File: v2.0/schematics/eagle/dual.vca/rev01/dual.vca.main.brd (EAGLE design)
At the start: 86 x 99 mm, 92 parts, among them IC1 TL082P, IC2 TL084P, IC3 LM324N, T1 BC547, T2 BC547, T3 BC547, T4 BC547, T5 BC547, T6 BC547

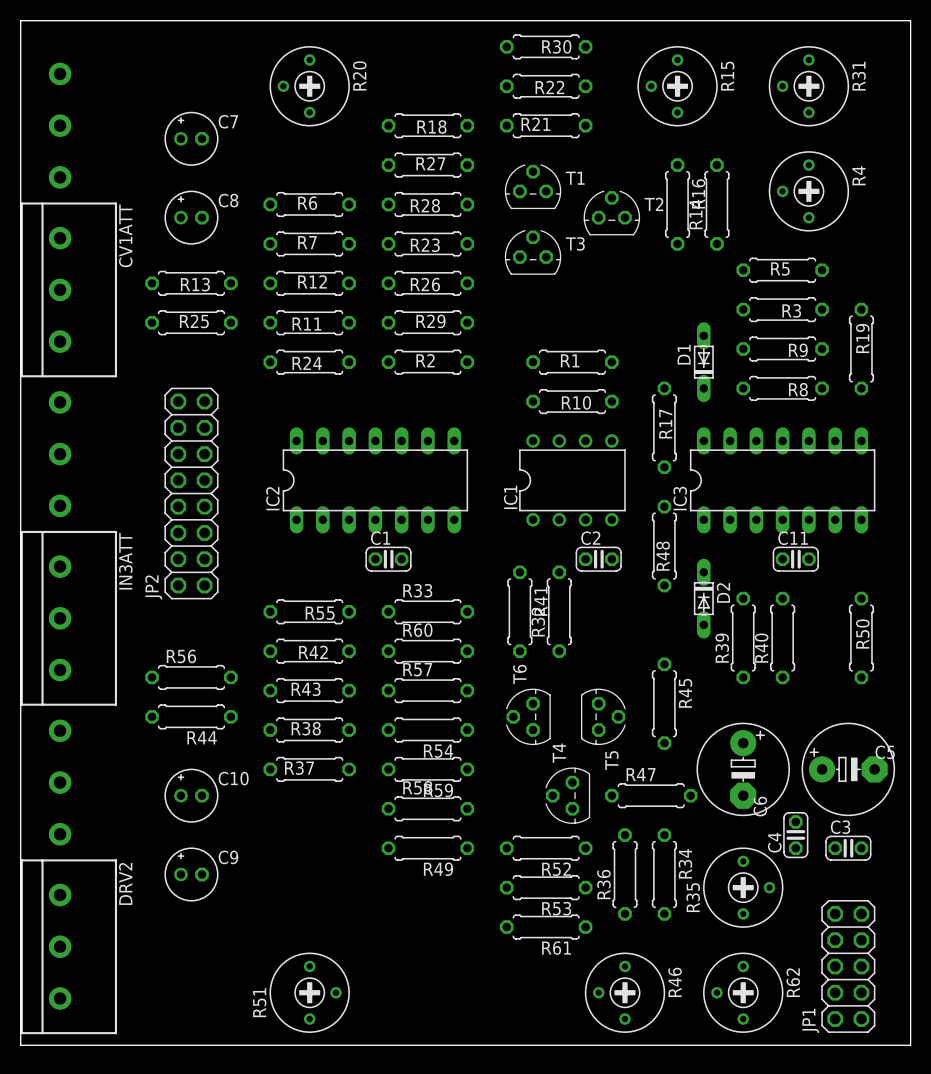
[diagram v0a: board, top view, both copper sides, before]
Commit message: Dual VCA autoroute and ground planes
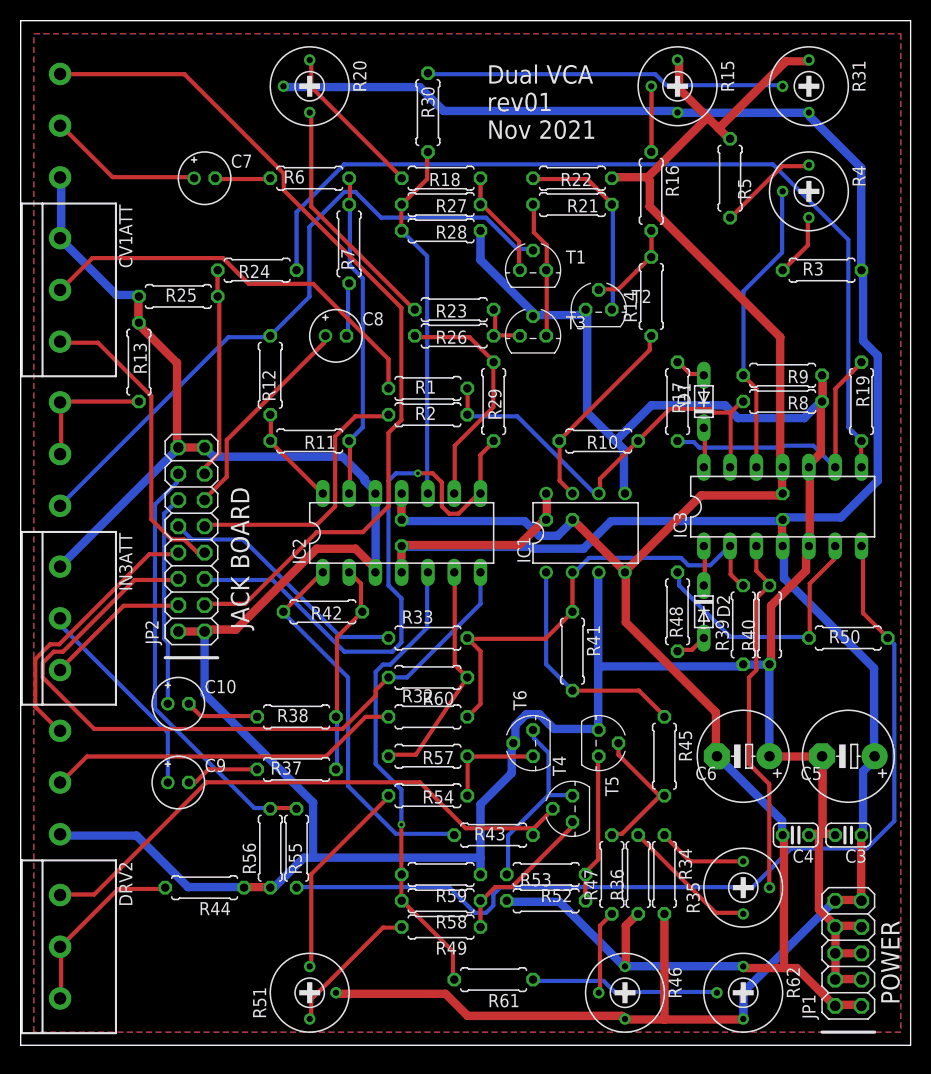
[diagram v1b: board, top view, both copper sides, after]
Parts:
- moved R55 22.9 mm to (26.7, 19.1), turned to 90 degrees
- moved R43 22.6 mm to (45.7, 20.3)
- moved R56 18.2 mm to (24.1, 19.1), turned to 90 degrees
- moved C8 18.1 mm to (30.5, 68.6)
- moved R44 16.6 mm to (17.8, 15.2)
- moved R32 16.3 mm to (39.4, 31.8), turned to 0 degrees
- moved R1 14.2 mm to (39.4, 63.5)
- moved R30 13.1 mm to (39.4, 90.2), turned to 270 degrees
- moved R11 11.4 mm to (27.9, 58.4)
- moved R14 10.9 mm to (61.0, 72.4)
- moved R24 10.2 mm to (22.9, 74.9)
- moved R59 10.2 mm to (40.6, 16.5)
- moved R5 10.2 mm to (68.6, 83.8), turned to 270 degrees
- moved R29 9.92 mm to (45.7, 62.2), turned to 270 degrees
- moved R12 9.67 mm to (24.1, 64.8), turned to 90 degrees
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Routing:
- net 0V: track 0.00 -> 362.5 mm
- net +12V: track 0.00 -> 268.6 mm
- net -12V: track 0.00 -> 204.0 mm
- net N$52: track 0.00 -> 91.1 mm
- net N$25: track 0.00 -> 86.4 mm
- net IN1: track 0.00 -> 84.8 mm
- net OUT3: track 0.00 -> 70.6 mm
- net N$4: track 0.00 -> 64.6 mm
- net OUT1: track 0.00 -> 57.1 mm, vias 0 -> 1
- net N$53: track 0.00 -> 55.5 mm
- net N$43: track 0.00 -> 45.1 mm
- net N$37: track 0.00 -> 45.1 mm, vias 0 -> 1
- net N$19: track 0.00 -> 42.6 mm
- net OUT4: track 0.00 -> 41.4 mm
- net N$29: track 0.00 -> 39.9 mm
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- added copper zone on layer 1, net 0V
- added copper zone on layer 16, net 0V
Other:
- board text added: "Dual VCA rev01 Nov 2021"
- board text added: "JACK BOARD"
- board text added: "POWER"

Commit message: Adjusted Dual.Seq comparrator
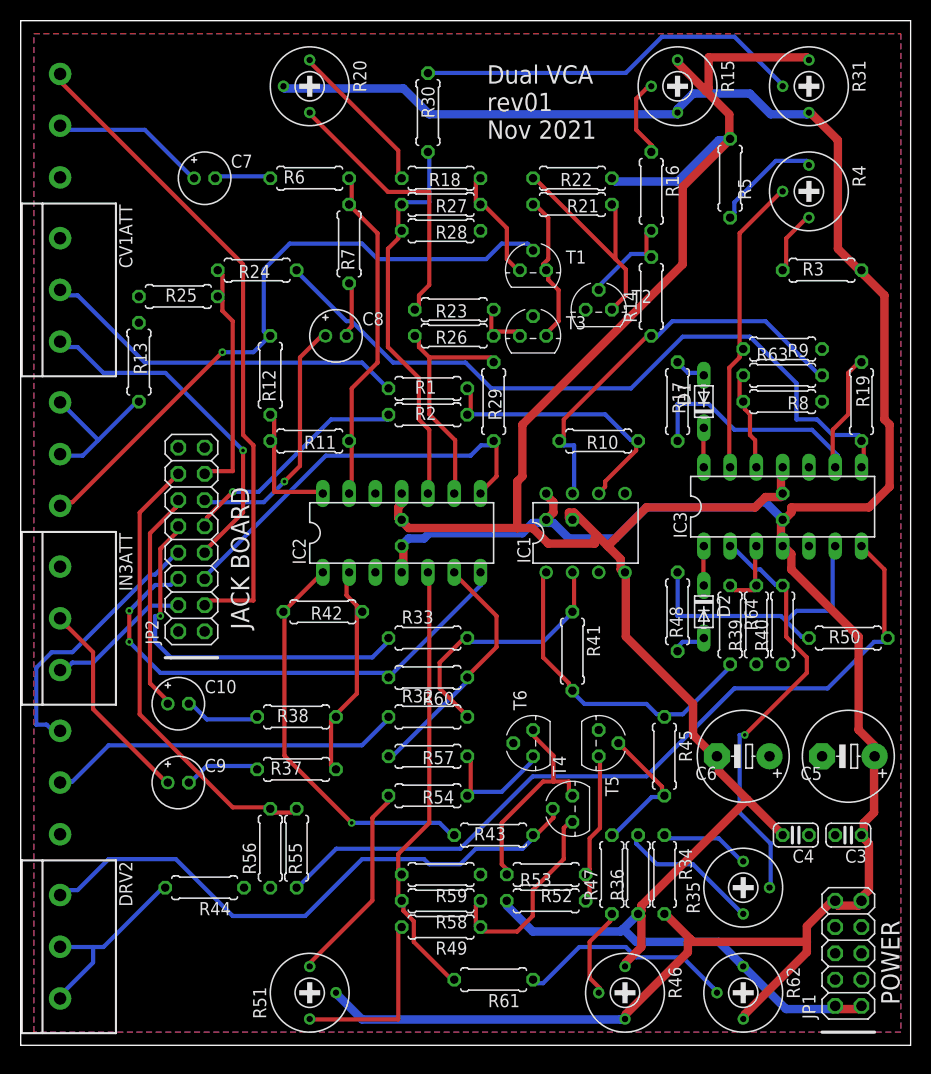
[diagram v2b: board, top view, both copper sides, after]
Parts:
- added R63, R64: 100K, _common:0207/7
- R1, R32: value 100K -> 65K
- moved R9 2.54 mm to (73.7, 67.3)
- moved R39 1.27 mm to (71.1, 40.6)
- moved R40 1.27 mm to (73.7, 40.6)
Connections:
- new net N$57: IC3.12, R63.1, R8.2
- new net N$58: IC3.2, R35.2, R40.2
- net N$17: now also R63.2
- net N$18: now also IC3.13; no longer IC3.12
- net N$19: no longer IC3.13, R8.2
- net N$42: now also R64.2
- net N$43: no longer IC3.2, R39.2
- net N$46: now also R39.2, R64.1; no longer R35.2, R40.2
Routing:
- net 0V: track 362.5 -> 0.00 mm
- net N$58: track 0.00 -> 41.0 mm, vias 0 -> 1
- net N$46: track 35.2 -> 7.00 mm
- net -12V: track 204.0 -> 231.5 mm
- net IN1: track 84.8 -> 63.6 mm
- net OUT3: track 70.6 -> 49.6 mm, vias 0 -> 2
- net N$17: track 19.4 -> 39.9 mm
- net N$43: track 45.1 -> 25.6 mm
- net OUT1: track 57.1 -> 39.4 mm, vias 1 -> 0
- net N$25: track 86.4 -> 70.8 mm
- net N$19: track 42.6 -> 27.3 mm
- net N$52: track 91.1 -> 77.2 mm
- net CV4: track 24.8 -> 36.5 mm, vias 0 -> 1
- net N$57: track 0.00 -> 9.74 mm
- net N$42: track 22.5 -> 31.4 mm
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
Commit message: Final board cams
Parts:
- JP1: value (none) -> PWR
- JP2: value (none) -> JACKBOARD
- renumbered R15 to CVINIT1, R20 to BAL1, R31 to OFS1, R35 to REF2, R4 to REF1, R46 to CVINIT2, R51 to BAL2, R62 to OFS2

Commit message: Added cam files; annotate panel schem with board edits; update cv resistor values
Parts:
- R1, R32: value 65K -> 56K
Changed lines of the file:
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@@
 <attribute name="VALUE" x="37.084" y="60.4012" locked="yes" size="1.27" layer="27" ratio="10"/>
 </element>
-<element name="R1" library="_common" package="0207/7" value="65K" x="39.37" y="63.5" locked="yes" smashed="yes">
+<element name="R1" library="_common" package="0207/7" value="56K" x="39.37" y="63.5" locked="yes" smashed="yes">
 <attribute name="NAME" x="38.1" y="62.992" locked="yes" size="1.27" layer="25" ratio="10"/>
 <attribute name="VALUE" x="37.084" y="62.9412" locked="yes" size="1.27" layer="27" ratio="10"/>
@@
 </element>
 <element name="R45" library="_common" package="0207/7" value="22K" x="62.23" y="27.94" locked="yes" smashed="yes" rot="R270">
-<attribute name="NAME" x="63.627" y="30.48" locked="yes" size="1.27" layer="25" ratio="10" rot="R270"/>
+<attribute name="NAME" x="61.722" y="29.21" locked="yes" size="1.27" layer="25" ratio="10" rot="R270"/>
 <attribute name="VALUE" x="61.6712" y="30.226" locked="yes" size="1.27" layer="27" ratio="10" rot="R270"/>
 </element>
@@
 <attribute name="VALUE" x="37.084" y="38.8112" locked="yes" size="1.27" layer="27" ratio="10"/>
 </element>
-<element name="R32" library="_common" package="0207/7" value="65K" x="39.37" y="31.75" locked="yes" smashed="yes">
+<element name="R32" library="_common" package="0207/7" value="56K" x="39.37" y="31.75" locked="yes" smashed="yes">
 <attribute name="NAME" x="37.465" y="31.242" locked="yes" size="1.27" layer="25" ratio="10"/>
 <attribute name="VALUE" x="37.084" y="31.1912" locked="yes" size="1.27" layer="27" ratio="10"/>
